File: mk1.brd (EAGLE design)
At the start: 114.3 x 76.2 mm, 28 parts, among them U1 IAM-20380, U2 MC34063AD, U3 ADXL345, U4 STM32F407VGT6

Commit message: Changed values of passive components around mc3406
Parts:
- C2: value 75uF -> 50000uf
- C3: value 20nf -> 200pf
- L1: value 308uH -> 50uh
- RSC: value 0.5ohm -> 0.75ohm
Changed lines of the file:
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@@
 <attribute name="VALUE" x="53.3908" y="11.1506" size="0.6096" layer="27" font="vector" ratio="20" rot="R90" align="top-center"/>
 </element>
-<element name="C2" library="SparkFun-Capacitors" package="EIA7343" value="75uF" x="42.0116" y="4.0132" smashed="yes">
+<element name="C2" library="SparkFun-Capacitors" package="EIA7343" value="50000uf" x="42.0116" y="4.0132" smashed="yes">
 <attribute name="NAME" x="42.0116" y="6.6802" size="0.6096" layer="25" font="vector" ratio="20" align="bottom-center"/>
 <attribute name="PROD_ID" value="CAP-07890" x="81.3816" y="-40.4368" size="1.778" layer="27" display="off"/>
@@
 <attribute name="VALUE" x="40.2844" y="64.3128" size="1.27" layer="27"/>
 </element>
-<element name="L1" library="SparkFun-Coils" package="0805" value="308uH" x="30.4546" y="19.05" smashed="yes" rot="R90">
+<element name="L1" library="SparkFun-Coils" package="0805" value="50uh" x="30.4546" y="19.05" smashed="yes" rot="R90">
 <attribute name="NAME" x="29.5656" y="19.05" size="0.6096" layer="25" font="vector" ratio="20" rot="R90" align="bottom-center"/>
 <attribute name="PROD_ID" value="NDUC-13076" x="87.6046" y="74.93" size="1.778" layer="27" rot="R90" display="off"/>
@@
 <attribute name="VALUE" x="60.6552" y="56.9214" size="0.6096" layer="27" font="vector" ratio="20" rot="R90" align="top-center"/>
 </element>
-<element name="RSC" library="SparkFun-Resistors" package="0805" value="0.5ohm" x="36.7538" y="22.5806" smashed="yes">
+<element name="RSC" library="SparkFun-Resistors" package="0805" value="0.75ohm" x="36.7538" y="22.5806" smashed="yes">
 <attribute name="NAME" x="36.7538" y="23.4696" size="0.6096" layer="25" font="vector" ratio="20" align="bottom-center"/>
 <attribute name="PROD_ID" value="RES-11622" x="71.0438" y="-40.9194" size="1.778" layer="27" display="off"/>
@@
 <attribute name="VALUE" x="99.2886" y="8.9916" size="0.6096" layer="27" font="vector" ratio="20" rot="R180" align="top-center"/>
 </element>
-<element name="C3" library="SparkFun-Capacitors" package="0805" value="20nf" x="29.845" y="15.367" smashed="yes" rot="R180">
+<element name="C3" library="SparkFun-Capacitors" package="0805" value="200pf" x="29.845" y="15.367" smashed="yes" rot="R180">
 <attribute name="NAME" x="29.845" y="14.478" size="0.6096" layer="25" font="vector" ratio="20" rot="R180" align="bottom-center"/>
 <attribute name="PROD_ID" value="CAP-08469" x="29.845" y="15.367" size="1.778" layer="27" rot="R180" display="off"/>

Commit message: Update Rev 1 with reroute
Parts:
- removed JP1: (no value), adafruit:1X03
- added C10: 22uF, SparkFun-Capacitors:0805
- added C9: 0.1uF, SparkFun-Capacitors:0603
- added J1, J2, J3: (no value), Wurth_Elektronik_Electromechanic_Board_to_Board_Connectors_rev18b:61300411121
- added LS1: CSS-0575A-SMT, CSS-0575A-SMT:CUI_CSS-0575A-SMT
- added R10, R11: 4.7k, SparkFun-Resistors:0603
- added R7: 200k, SparkFun-Resistors:0603
- added R8: 220k, SparkFun-Resistors:0603
- added R9: 43k, SparkFun-Resistors:0603
- added U5: LT1529CQTRPBF, LT1529CQTRPBF:DDPAK-5_Q
- added U6: MPL115A2, MPL115A2:LGA8
- added U7: SN65HVD232DR, SN65HVD232DR:SOIC127P600X175-8N
- C1: device SparkFun-Capacitors:EIA7343 -> SparkFun-Capacitors:1206-POLAR
- C2: value 50000uf -> 100uF; device SparkFun-Capacitors:EIA7343 -> SparkFun-Capacitors:1206-POLAR
- C5: value 2.2uf -> 100uF; device SparkFun-Capacitors:EIA7343 -> SparkFun-Capacitors:1206-POLAR
- L1: value 50uh -> 47uh
- moved BT2 87.9 mm to (11.4, 36.8)
- moved BT1 87.6 mm to (100.3, 36.8)
- moved C1 62.9 mm to (29.8, 70.5), turned to 270 degrees
- moved R1 60.5 mm to (43.7, 70.1), turned to 0 degrees
- moved C2 59.4 mm to (43.7, 63.4), turned to 180 degrees
- moved LED1 58.8 mm to (32.9, 16.4), turned to 0 degrees
- moved R2 56.3 mm to (43.7, 66.9)
- moved LED2 53.9 mm to (32.9, 19.7), turned to 0 degrees
- moved R3 51.6 mm to (38.4, 16.4), turned to 180 degrees
- moved U2 51.4 mm to (38.1, 67.6), turned to 0 degrees
- moved LED3 49.2 mm to (32.9, 22.9), turned to 0 degrees
- moved RSC 48.9 mm to (33.3, 71.4), turned to 90 degrees
- moved D1 48.6 mm to (48.4, 60.3)
- moved L1 47.8 mm to (48.4, 63.4), turned to 180 degrees
- moved R4 46.7 mm to (38.4, 19.7), turned to 180 degrees
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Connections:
- removed net N$15: JP1.2, U4.72
- removed net N$16: JP1.1, U4.76
- removed net N$6: C7.1, U1.1, U3.1
- new net +3V3: C7.1, U1.1, U3.1, U6.1, U7.3
- new net BENABLE: U4.56, U6.5
- new net BSCL: R11.2, U4.92, U6.8
- new net BSDA: R10.2, U4.93, U6.7
- new net BSHD: U6.4
- new net BUZZER: LS1.1, U4.37
- new net CANH: J3.2, U7.7
- new net CANL: J3.1, U7.6
- new net CANRX: U4.70, U7.4
- new net CANTX: U4.71, U7.1
- new net JTCK: J3.3, U4.76
- new net N$18: R7.1, R8.2, U5.2
- new net N$19: R8.1, R9.2
- new net N$22: C9.2, U6.2
- new net S1IN: J1.2, U4.34
- new net S1O: J1.3, U4.33
- new net S2IN: J2.2, U4.36
- new net S2O: J2.3, U4.35
- new net SERVOPWR: U4.57, U5.4
- new net SWDIO: J3.4, U4.72
- new net V7+: C10.2, J1.4, J2.4, R7.2, U5.1
- net 3.3V: now also C2.1, C5.1; no longer C2.A, C5.A
- net BATIN: now also C1.1, U5.5; no longer C1.A
- net GND: now also C1.2, C10.1, C2.2, C5.2, C9.1, J1.1, J2.1, LS1.2, R10.1, R11.1, R9.1, U5.3, U6.3, U7.2; no longer C1.C, C2.C, C5.C
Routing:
- net GND: track 53.1 -> 457.1 mm, vias 4 -> 12
- net V7+: track 0.00 -> 135.3 mm, vias 0 -> 4
- net +3V3: track 0.00 -> 81.1 mm, vias 0 -> 7
- net SERVOPWR: track 0.00 -> 73.9 mm, vias 0 -> 2
- net N$6: track 68.2 -> 0.00 mm, vias 2 -> 0
- net S1O: track 0.00 -> 55.7 mm, vias 0 -> 4
- net JTCK: track 0.00 -> 54.8 mm, vias 0 -> 2
- net S1IN: track 0.00 -> 53.1 mm, vias 0 -> 2
- net SWDIO: track 0.00 -> 49.4 mm, vias 0 -> 2
- net S2IN: track 0.00 -> 47.7 mm, vias 0 -> 2
- net CANL: track 0.00 -> 45.6 mm, vias 0 -> 2
- net S2O: track 0.00 -> 44.2 mm
- net BUZZER: track 0.00 -> 40.9 mm, vias 0 -> 2
- net CANH: track 0.00 -> 40.2 mm
- net SSG: track 53.0 -> 16.5 mm
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- removed copper zone on layer 1, net GND
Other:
- board size 114.3 x 76.2 mm -> 113 x 73.8 mm
- board text added: "Rocket Mk 1.0 Rev 1.0 Robert Murphy & Dawson Moore"

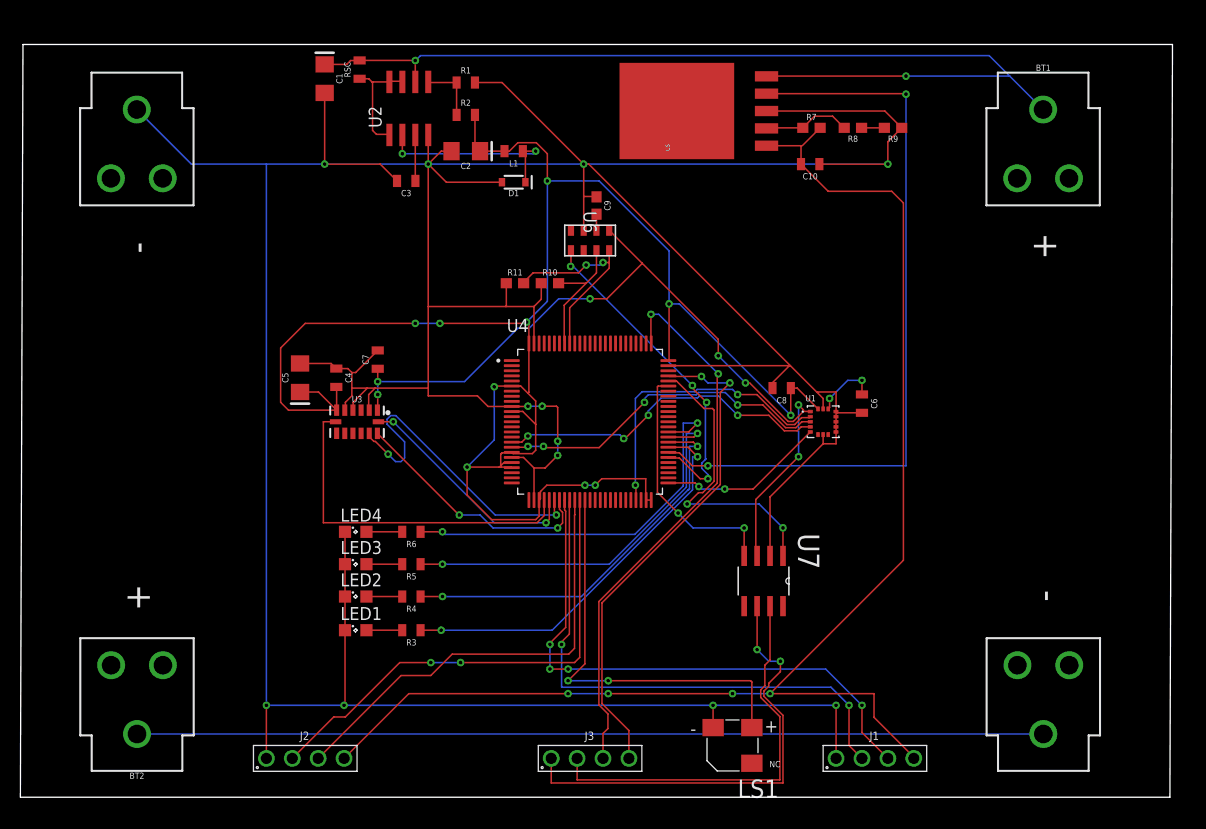
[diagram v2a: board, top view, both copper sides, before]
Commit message: Added silkscreen names/logo
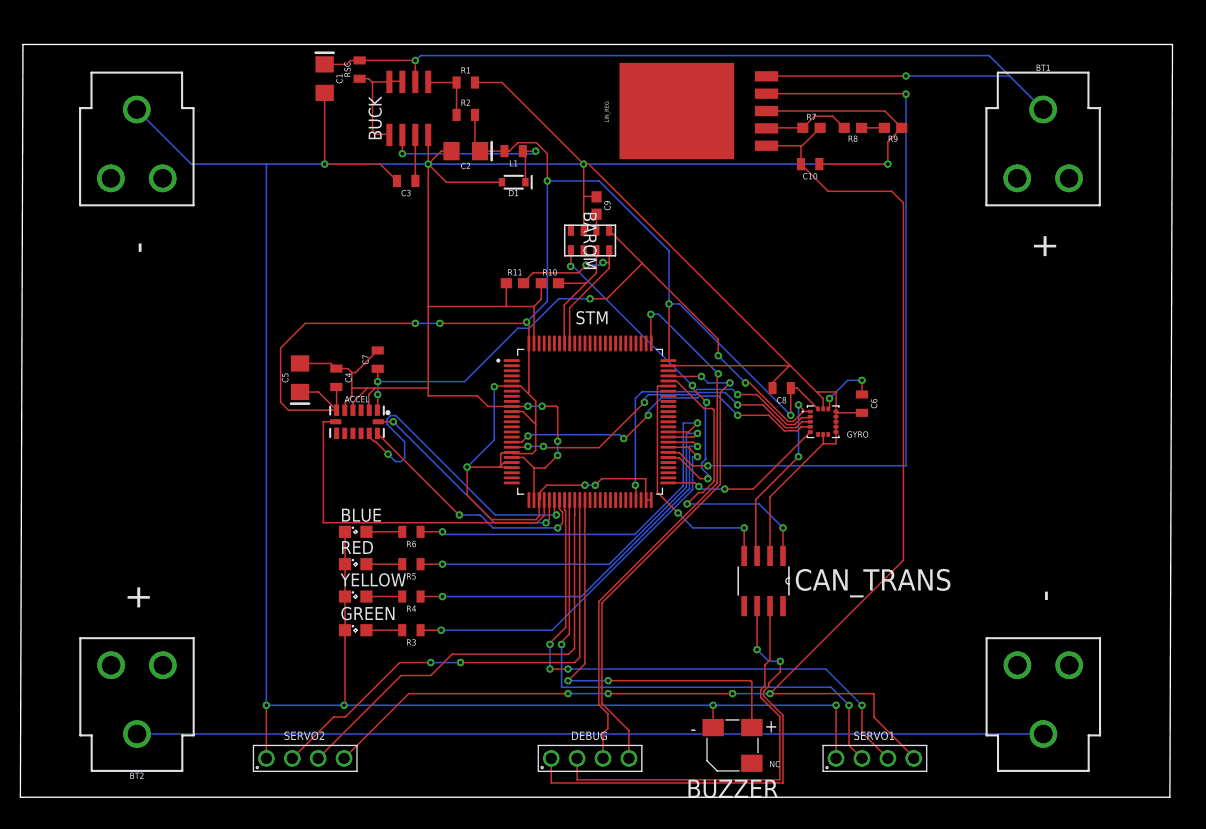
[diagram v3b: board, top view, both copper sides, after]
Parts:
- renumbered J1 to SERVO1, J2 to SERVO2, J3 to DEBUG, LED1 to GREEN, LED2 to YELLOW, LED3 to RED, LED4 to BLUE, LS1 to BUZZER, U1 to GYRO, U2 to BUCK, U3 to ACCEL, U4 to STM, U5 to LIN_REG, U6 to BAROM, U7 to CAN_TRANS
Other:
- board text added: "C:/Users/rwmur/Documents/RRaP/PurdueP.bmp"
